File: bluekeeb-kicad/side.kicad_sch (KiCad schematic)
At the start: 68 parts, among them SW1 SW_Push, SW11 SW_Push, SW13 SW_Push, SW15 SW_Push, SW17 SW_Push, SW19 SW_Push, SW21 SW_Push, SW23 SW_Push, SW25 SW_Push, SW27 SW_Push, SW29 SW_Push, SW3 SW_Push, SW31 SW_Push, SW33 SW_Push, SW35 SW_Push, SW37 SW_Push, SW39 SW_Push, SW41 SW_Push, SW43 SW_Push, SW45 SW_Push, SW47 SW_Push, SW49 SW_Push, SW5 SW_Push, SW51 SW_Push, SW53 SW_Push, SW55 SW_Push, SW57 SW_Push, SW59 SW_Push, SW7 SW_Push, SW9 SW_Push, U1 XIAO-nRF52840-SMD

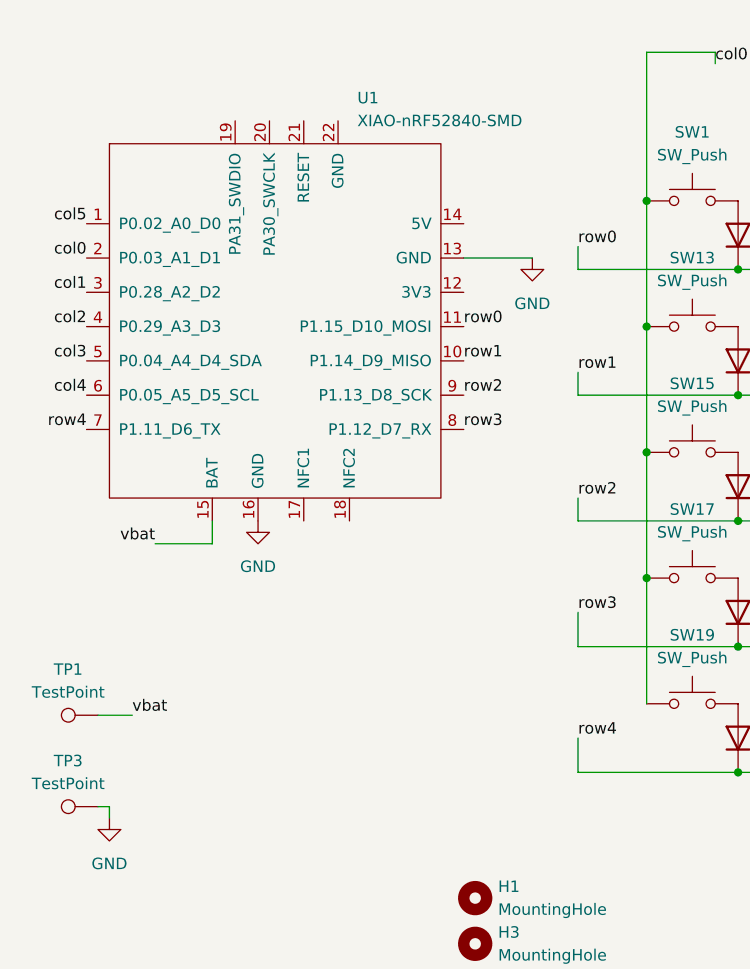
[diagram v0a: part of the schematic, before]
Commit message: Finalllyyy i fixed my mousebites problem
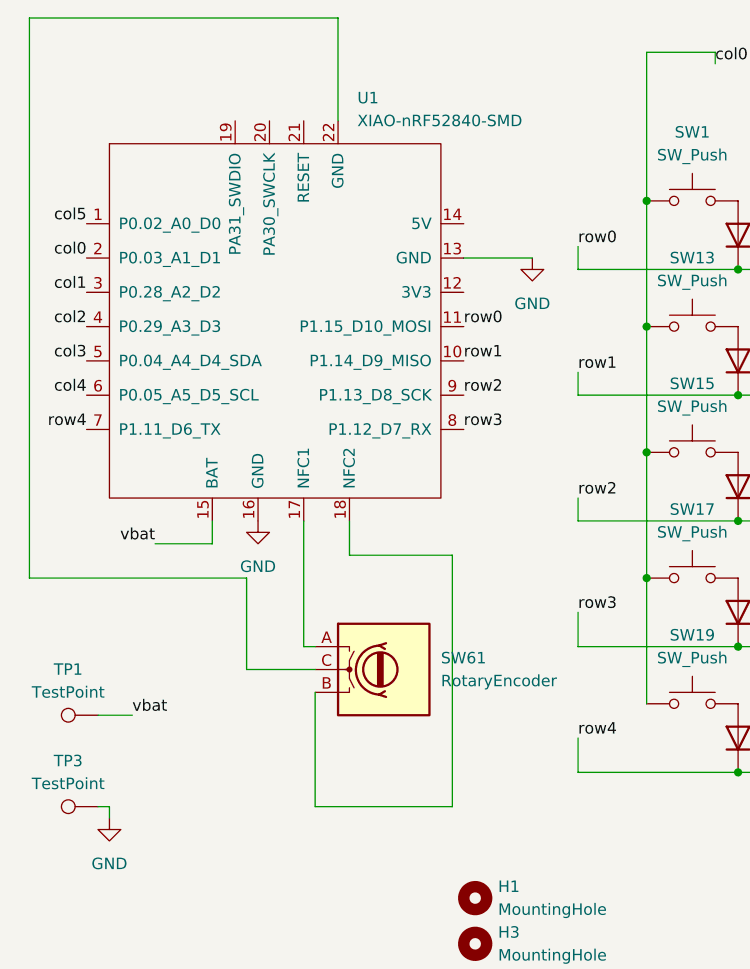
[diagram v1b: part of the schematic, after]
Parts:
- added SW61: RotaryEncoder, Rotary_Encoder:RotaryEncoder_Alps_EC11E-Switch_Vertical_H20mm, symbol Device:RotaryEncoder
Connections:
- net at U1.17 (NFC1): now also SW61.A
- net at U1.18 (NFC2): now also SW61.B
- net at U1.22 (GND): now also SW61.C
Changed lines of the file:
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@@
 	(wire
 		(pts
+			(xy 124.46 116.84) (xy 124.46 102.87)
+		)
+		(stroke
+			(width 0)
+			(type default)
+		)
+	)
+	(wire
+		(pts
 			(xy 162.56 50.8) (xy 170.18 50.8)
 		)
@@
 	(wire
 		(pts
+			(xy 118.11 109.22) (xy 93.98 109.22)
+		)
+		(stroke
+			(width 0)
+			(type default)
+		)
+	)
+	(wire
+		(pts
 			(xy 260.35 88.9) (xy 243.84 88.9)
 		)
@@
 	(wire
 		(pts
+			(xy 118.11 119.38) (xy 118.11 109.22)
+		)
+		(stroke
+			(width 0)
+			(type default)
+		)
+	)
+	(wire
+		(pts
+			(xy 140.97 134.62) (xy 140.97 106.68)
+		)
+		(stroke
+			(width 0)
+			(type default)
+		)
+	)
+	(wire
+		(pts
 			(xy 191.77 74.93) (xy 172.72 74.93)
 		)
@@
 	(wire
 		(pts
+			(xy 125.73 116.84) (xy 124.46 116.84)
+		)
+		(stroke
+			(width 0)
+			(type default)
+		)
+	)
+	(wire
+		(pts
+			(xy 125.73 121.92) (xy 125.73 134.62)
+		)
+		(stroke
+			(width 0)
+			(type default)
+		)
+	)
+	(wire
+		(pts
+			(xy 125.73 119.38) (xy 118.11 119.38)
+		)
+		(stroke
+			(width 0)
+			(type default)
+		)
+	)
+	(wire
+		(pts
 			(xy 209.55 74.93) (xy 191.77 74.93)
 		)
@@
 	(wire
 		(pts
+			(xy 128.27 46.99) (xy 128.27 58.42)
+		)
+		(stroke
+			(width 0)
+			(type default)
+		)
+	)
+	(wire
+		(pts
 			(xy 191.77 130.81) (xy 172.72 130.81)
 		)
@@
 	(wire
 		(pts
+			(xy 129.54 106.68) (xy 129.54 102.87)
+		)
+		(stroke
+			(width 0)
+			(type default)
+		)
+	)
+	(wire
+		(pts
 			(xy 199.39 50.8) (xy 200.66 50.8)
 		)
@@
 	(wire
 		(pts
+			(xy 93.98 109.22) (xy 93.98 46.99)
+		)
+		(stroke
+			(width 0)
+			(type default)
+		)
+	)
+	(wire
+		(pts
 			(xy 217.17 67.31) (xy 217.17 50.8)
 		)
@@
 	(wire
 		(pts
+			(xy 140.97 106.68) (xy 129.54 106.68)
+		)
+		(stroke
+			(width 0)
+			(type default)
+		)
+	)
+	(wire
+		(pts
 			(xy 172.72 74.93) (xy 154.94 74.93)
 		)
@@
 	(wire
 		(pts
+			(xy 93.98 46.99) (xy 128.27 46.99)
+		)
+		(stroke
+			(width 0)
+			(type default)
+		)
+	)
+	(wire
+		(pts
 			(xy 181.61 67.31) (xy 181.61 50.8)
 		)
@@
 	(wire
 		(pts
+			(xy 125.73 134.62) (xy 140.97 134.62)
+		)
+		(stroke
+			(width 0)
+			(type default)
+		)
+	)
+	(wire
+		(pts
 			(xy 114.3 105.41) (xy 114.3 102.87)
 		)
@@
 					(unit 1)
 				)
+			)
+		)
+	)
+	(symbol
+		(lib_id "Device:RotaryEncoder")
+		(at 133.35 119.38 0)
+		(unit 1)
+		(exclude_from_sim no)
+		(in_bom yes)
+		(on_board yes)
+		(dnp no)
+		(fields_autoplaced yes)
+		(property "Reference" "SW61"
+			(at 139.7 118.1099 0)
+			(effects
+				(font
+					(size 1.27 1.27)
+				)
+				(justify left)
+			)
+		)
+		(property "Value" "RotaryEncoder"
+			(at 139.7 120.6499 0)
+			(effects
+				(font
+					(size 1.27 1.27)
+				)
+				(justify left)
+			)
+		)
+		(property "Footprint" "Rotary_Encoder:RotaryEncoder_Alps_EC11E-Switch_Vertical_H20mm"
+			(at 129.54 115.316 0)
+			(effects
+				(font
+					(size 1.27 1.27)
+				)
+				(hide yes)
+			)
+		)
+		(property "Datasheet" "~"
+			(at 133.35 112.776 0)
+			(effects
+				(font
+					(size 1.27 1.27)
+				)
+				(hide yes)
+			)
+		)
+		(property "Description" "Rotary encoder, dual channel, incremental quadrate outputs"
+			(at 133.35 119.38 0)
+			(effects
+				(font
+					(size 1.27 1.27)
+				)
+				(hide yes)
+			)
+		)
+		(pin "B"
+		)
+		(pin "A"
+		)
+		(pin "C"
+		)
+		(instances
+			(project ""
+				(path "/9c7c3d7f-df07-44e3-9769-a5f86c49873c/12ef109c-a2f1-40c4-8500-95466df51b75"
+					(reference "SW62")
+					(unit 1)
+				)
+				(path "/9c7c3d7f-df07-44e3-9769-a5f86c49873c/727cb513-7415-499b-80c9-83fd548ec377"
+					(reference "SW61")
+					(unit 1)
+				)

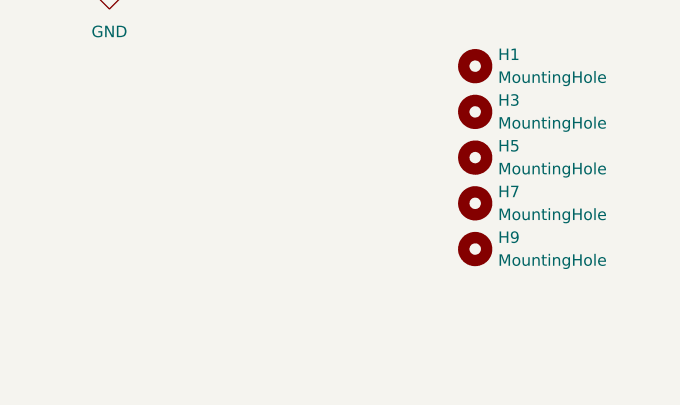
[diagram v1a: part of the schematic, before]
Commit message: added some mounting holes, and i moved the testpoints to a different location.
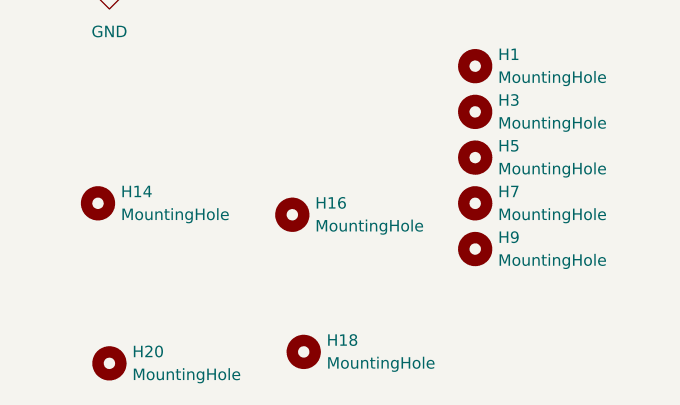
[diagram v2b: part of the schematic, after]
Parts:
- added H14, H16, H18, H20: MountingHole, MountingHole:MountingHole_2.2mm_M2, symbol Mechanical:MountingHole
